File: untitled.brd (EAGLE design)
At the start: 41.6 x 28.6 mm, 21 parts, among them IC1 ACS758LCB-050B-PFF-T

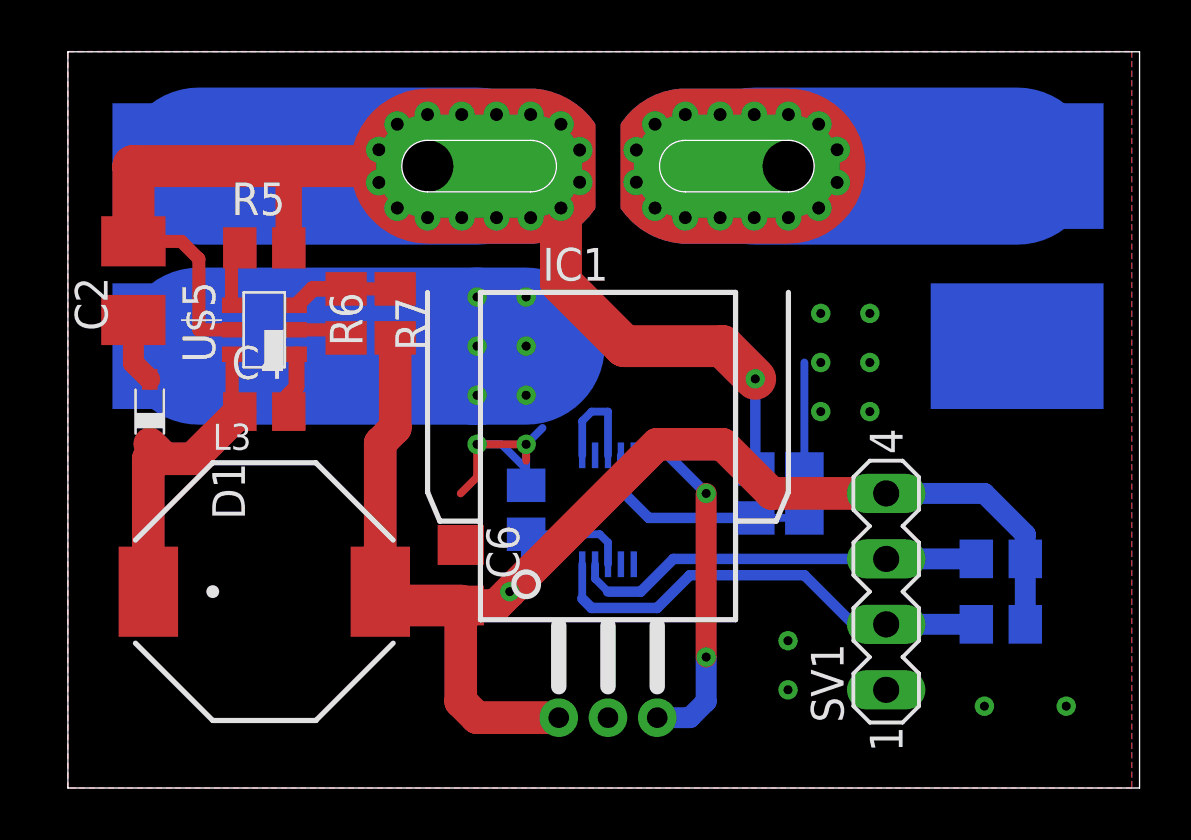
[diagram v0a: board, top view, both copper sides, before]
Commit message: Add TVS to power module
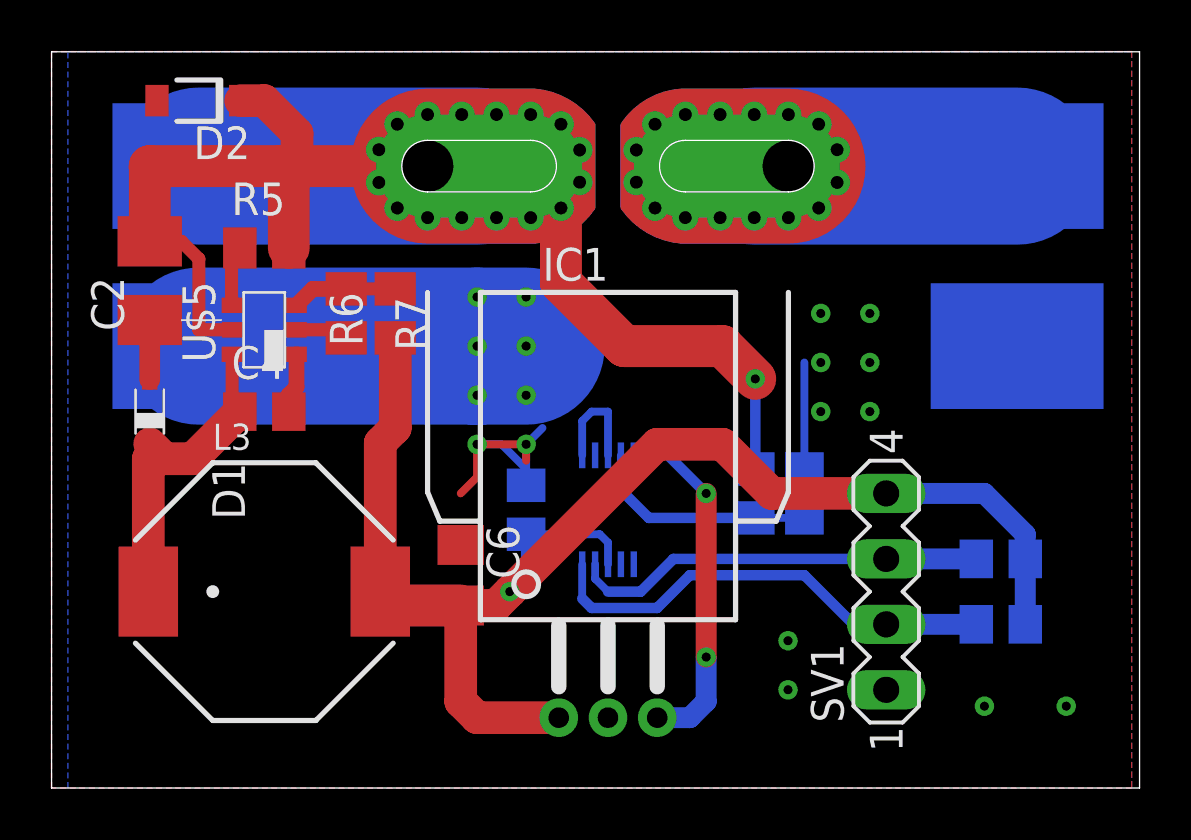
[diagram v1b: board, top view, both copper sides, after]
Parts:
- added D2: SMF5.0AT1, diode:SOD123FL
- moved C2 0.63 mm to (19.7, 34.9)
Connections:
- net GND: now also D2.A
- net N$4: now also D2.C
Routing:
- net N$4: track 58.3 -> 71.0 mm
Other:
- board size 41.6 x 28.6 mm -> 42.2 x 28.6 mm
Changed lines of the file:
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@@
 <layer number="18" name="Vias" color="2" fill="1" visible="yes" active="yes"/>
 <layer number="19" name="Unrouted" color="6" fill="1" visible="yes" active="yes"/>
-<layer number="20" name="Dimension" color="24" fill="1" visible="no" active="yes"/>
+<layer number="20" name="Dimension" color="24" fill="1" visible="yes" active="yes"/>
 <layer number="21" name="tPlace" color="7" fill="1" visible="yes" active="yes"/>
 <layer number="22" name="bPlace" color="7" fill="1" visible="yes" active="yes"/>
 <layer number="23" name="tOrigins" color="15" fill="1" visible="yes" active="yes"/>
 <layer number="24" name="bOrigins" color="15" fill="1" visible="yes" active="yes"/>
-<layer number="25" name="tNames" color="7" fill="1" visible="no" active="yes"/>
-<layer number="26" name="bNames" color="7" fill="1" visible="no" active="yes"/>
-<layer number="27" name="tValues" color="7" fill="1" visible="no" active="yes"/>
+<layer number="25" name="tNames" color="7" fill="1" visible="yes" active="yes"/>
+<layer number="26" name="bNames" color="7" fill="1" visible="yes" active="yes"/>
+<layer number="27" name="tValues" color="7" fill="1" visible="yes" active="yes"/>
 <layer number="28" name="bValues" color="7" fill="1" visible="no" active="yes"/>
 <layer number="29" name="tStop" color="7" fill="3" visible="no" active="yes"/>
@@
 <board>
 <plain>
-<wire x1="16.51" y1="15.24" x2="58.09" y2="15.24" width="0" layer="20"/>
+<wire x1="15.875" y1="15.24" x2="58.09" y2="15.24" width="0" layer="20"/>
 <wire x1="58.09" y1="15.24" x2="58.09" y2="43.805" width="0" layer="20"/>
-<wire x1="58.09" y1="43.805" x2="16.51" y2="43.805" width="0" layer="20"/>
-<wire x1="16.51" y1="43.805" x2="16.51" y2="15.24" width="0" layer="20"/>
+<wire x1="58.09" y1="43.805" x2="15.875" y2="43.805" width="0" layer="20"/>
+<wire x1="15.875" y1="43.805" x2="15.875" y2="15.24" width="0" layer="20"/>
 <text x="15.24" y="19.05" size="1.778" layer="26" ratio="18" rot="MR0" align="bottom-right">esk8pal
 v0.1.0
@@
 <attribute name="VALUE" x="21.685" y="28.195" size="1.27" layer="27" rot="R90"/>
 </element>
-<element name="C2" library="rcl" library_urn="urn:adsk.eagle:library:334" package="B/3528-21R" package3d_urn="urn:adsk.eagle:package:23409/2" value="2.2uF 100V" x="19.05" y="34.925" smashed="yes" rot="R90">
-<attribute name="NAME" x="18.05" y="32.975" size="1.27" layer="25" rot="R90"/>
-<attribute name="POPULARITY" value="1" x="19.05" y="34.925" size="1.778" layer="27" rot="R90" display="off"/>
-<attribute name="SPICEPREFIX" value="C" x="19.05" y="34.925" size="1.778" layer="27" rot="R90" display="off"/>
-<attribute name="VALUE" x="21.375" y="32.975" size="1.27" layer="27" rot="R90"/>
+<element name="C2" library="rcl" library_urn="urn:adsk.eagle:library:334" package="B/3528-21R" package3d_urn="urn:adsk.eagle:package:23409/2" value="2.2uF 100V" x="19.685" y="34.925" smashed="yes" rot="R90">
+<attribute name="NAME" x="18.685" y="32.975" size="1.27" layer="25" rot="R90"/>
+<attribute name="POPULARITY" value="1" x="19.685" y="34.925" size="1.778" layer="27" rot="R90" display="off"/>
+<attribute name="SPICEPREFIX" value="C" x="19.685" y="34.925" size="1.778" layer="27" rot="R90" display="off"/>
+<attribute name="VALUE" x="22.01" y="32.975" size="1.27" layer="27" rot="R90"/>
 </element>
 <element name="C6" library="rcl" library_urn="urn:adsk.eagle:library:334" package="R/2012-12R" package3d_urn="urn:adsk.eagle:package:23426/2" value="22uF 25V" x="31.75" y="23.495" smashed="yes" rot="R270">
@@
 <attribute name="NAME" x="22.13" y="28.36" size="1.016" layer="25" ratio="18"/>
 <attribute name="VALUE" x="22.13" y="16.61" size="0.8128" layer="27" ratio="10"/>
+</element>
+<element name="D2" library="diode" library_urn="urn:adsk.eagle:library:210" package="SOD123FL" package3d_urn="urn:adsk.eagle:package:43458/1" value="SMF5.0AT1" x="21.59" y="41.91" smashed="yes" rot="R180">
+<attribute name="NAME" x="23.59" y="40.91" size="1.27" layer="25" rot="R180"/>
+<attribute name="POPULARITY" value="2" x="21.59" y="41.91" size="1.778" layer="27" rot="R180" display="off"/>
+<attribute name="VALUE" x="23.59" y="44.41" size="1.27" layer="27" rot="R180"/>
 </element>
 </elements>
@@
 <contactref element="C2" pad="-"/>
 <contactref element="C6" pad="-"/>
-<wire x1="19.05" y1="33.4" x2="19.05" y2="31.73" width="0.8128" layer="1"/>
-<wire x1="19.05" y1="31.73" x2="19.685" y2="31.095" width="0.8128" layer="1"/>
+<wire x1="19.685" y1="33.4" x2="19.685" y2="31.095" width="0.8128" layer="1"/>
 <wire x1="25.38" y1="33.02" x2="26.99" y2="33.02" width="0.508" layer="1"/>
 <wire x1="26.99" y1="33.02" x2="27.305" y2="32.705" width="0.508" layer="1"/>
 <polygon width="0.508" layer="1" isolate="0.4064">
-<vertex x="16.51" y="43.815"/>
+<vertex x="15.875" y="43.815"/>
 <vertex x="57.785" y="43.815"/>
 <vertex x="57.785" y="15.24"/>
-<vertex x="16.51" y="15.24"/>
+<vertex x="15.875" y="15.24"/>
 </polygon>
 <wire x1="34.29" y1="32.385" x2="32.385" y2="32.385" width="6.096" layer="16"/>
@@
 <via x="47.625" y="29.845" extent="1-16" drill="0.35"/>
 <via x="45.72" y="29.845" extent="1-16" drill="0.35"/>
+<contactref element="D2" pad="A"/>
 </signal>
 <signal name="VCC">
@@
 <contactref element="R5" pad="2"/>
 <contactref element="U$5" pad="5"/>
-<wire x1="33.02" y1="38.735" x2="31.115" y2="40.64" width="1.016" layer="1"/>
+<wire x1="33.02" y1="38.735" x2="32.0675" y2="39.6875" width="1.016" layer="1"/>
 <contactref element="C2" pad="+"/>
+<wire x1="32.0675" y1="39.6875" x2="31.115" y2="40.64" width="1.016" layer="1"/>
 <wire x1="21.59" y1="39.37" x2="32.385" y2="39.37" width="6.096" layer="16"/>
 <wire x1="35.64" y1="37.745" x2="35.64" y2="34.845" width="1.6256" layer="1"/>
 <wire x1="35.64" y1="34.845" x2="38.1" y2="32.385" width="1.6256" layer="1"/>
-<wire x1="30.465" y1="39.37" x2="25.08" y2="39.37" width="1.6256" layer="1"/>
-<wire x1="24.765" y1="39.37" x2="19.05" y2="39.37" width="1.6256" layer="1"/>
-<wire x1="19.05" y1="39.37" x2="19.05" y2="36.45" width="1.6256" layer="1"/>
+<wire x1="19.685" y1="36.45" x2="19.685" y2="39.37" width="1.6256" layer="1"/>
 <wire x1="22.88" y1="33.02" x2="21.59" y2="33.02" width="0.508" layer="1"/>
-<wire x1="20.91" y1="36.45" x2="19.05" y2="36.45" width="0.508" layer="1"/>
+<wire x1="20.91" y1="36.45" x2="19.685" y2="36.45" width="0.508" layer="1"/>
 <wire x1="21.59" y1="35.77" x2="20.91" y2="36.45" width="0.508" layer="1"/>
 <wire x1="21.59" y1="33.02" x2="21.59" y2="35.77" width="0.508" layer="1"/>
@@
 <wire x1="41.91" y1="32.385" x2="38.1" y2="32.385" width="1.6256" layer="1"/>
 <wire x1="43.18" y1="27.62" x2="43.18" y2="31.115" width="0.4064" layer="16"/>
-<wire x1="25.08" y1="36.195" x2="25.08" y2="39.37" width="1.016" layer="1"/>
+<wire x1="25.08" y1="36.195" x2="25.08" y2="39.37" width="1.6256" layer="1"/>
+<contactref element="D2" pad="C"/>
+<wire x1="19.685" y1="39.37" x2="22.225" y2="39.37" width="1.6256" layer="1"/>
+<wire x1="33.02" y1="39.37" x2="33.655" y2="39.37" width="1.6256" layer="1"/>
+<wire x1="24.765" y1="39.37" x2="25.4" y2="39.37" width="1.6256" layer="1"/>
+<wire x1="25.4" y1="39.37" x2="31.115" y2="39.37" width="0.508" layer="1"/>
+<wire x1="31.115" y1="39.37" x2="33.02" y2="39.37" width="0.508" layer="1"/>
+<wire x1="22.225" y1="39.37" x2="24.765" y2="39.37" width="1.6256" layer="1"/>
+<wire x1="31.75" y1="39.37" x2="32.0675" y2="39.6875" width="1.27" layer="1"/>
+<wire x1="23.215" y1="41.91" x2="24.13" y2="41.91" width="1.27" layer="1"/>
+<wire x1="25.4" y1="40.64" x2="25.4" y2="39.37" width="1.27" layer="1"/>
+<wire x1="24.13" y1="41.91" x2="25.4" y2="40.64" width="1.27" layer="1"/>
+<wire x1="25.08" y1="39.37" x2="31.115" y2="39.37" width="1.6256" layer="1"/>
 <wire x1="33.655" y1="38.735" x2="33.02" y2="38.735" width="0" layer="19" extent="1-16"/>
-<wire x1="24.765" y1="39.37" x2="21.59" y2="39.37" width="0" layer="19" extent="1-16"/>
+<wire x1="33.655" y1="39.37" x2="33.655" y2="38.735" width="0" layer="19" extent="1-16"/>
 </signal>
 <signal name="N$5">

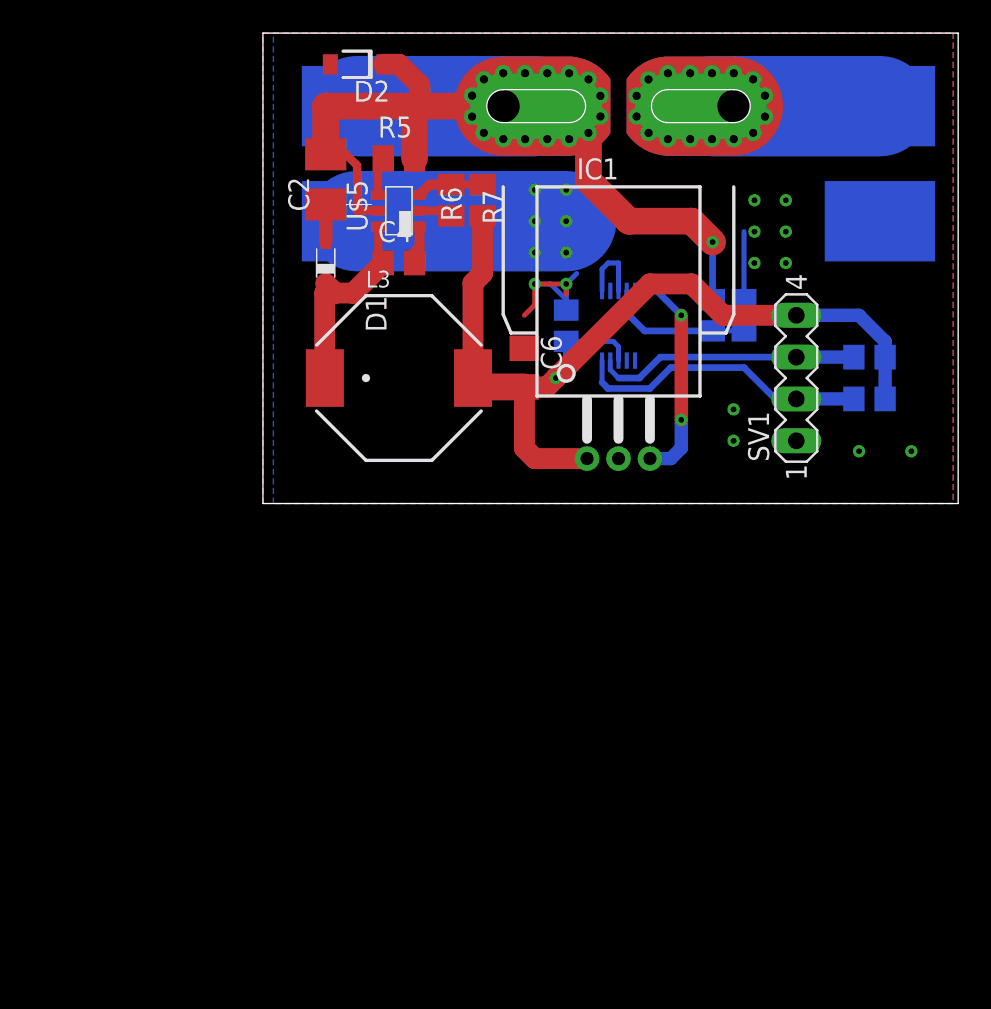
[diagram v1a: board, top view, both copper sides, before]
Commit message: Update scheamictic to include dedicated ldo for senors and p mosfeto control power for sensors
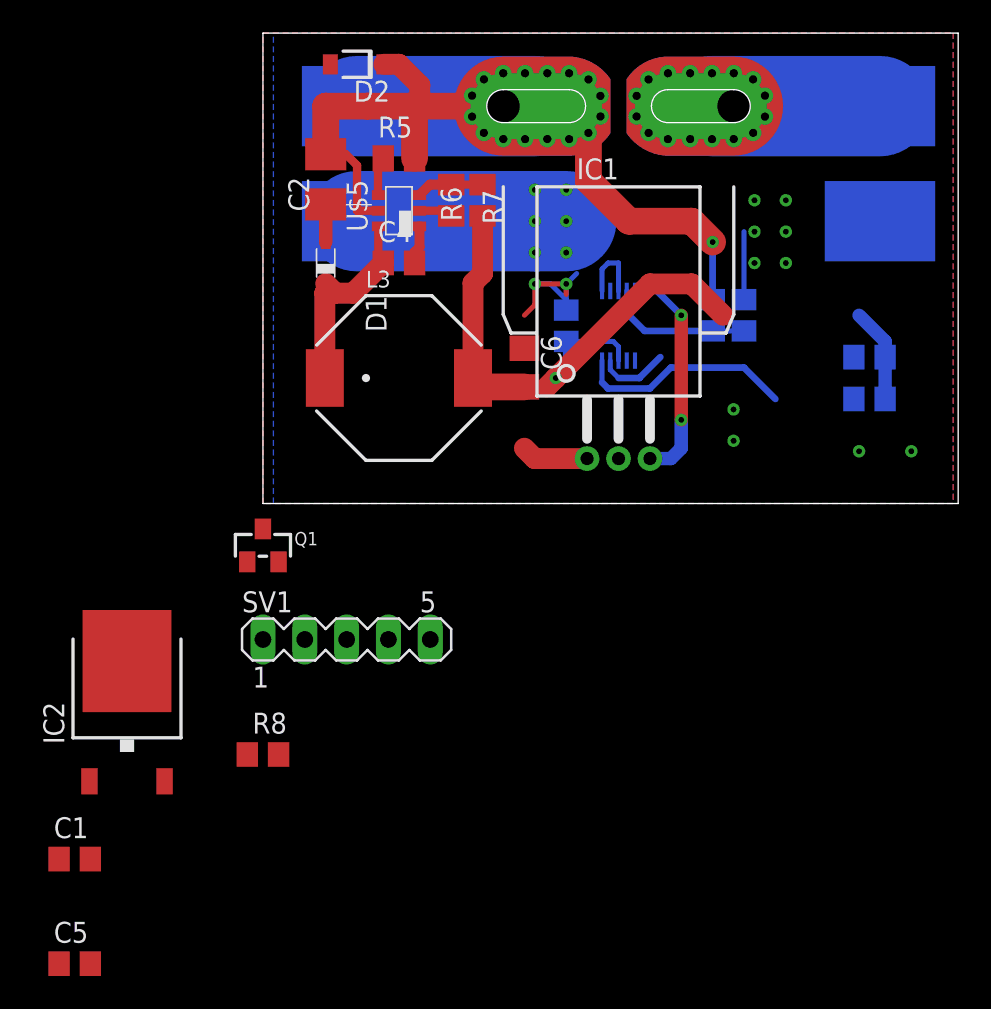
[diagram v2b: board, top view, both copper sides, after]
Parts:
- added C1, C5: 100nF, rcl:C0805
- added IC2: LM2936DT-3.3, national-semiconductor:TO252
- added Q1: (no value), microbuilder:SOT23-WIDE
- added R8: 100k, rcl:R0805
- SV1: device con-lstb:MA04-1 -> con-lstb:MA05-1
- moved SV1 31.6 mm to (21.0, 6.99), turned to 0 degrees
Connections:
- new net N$12: C1.1, IC2.3, Q1.2, R8.1
- new net N$7: Q1.1, R8.2, SV1.5
- new net N$8: C6.+, L3.2, R6.1, SV1.4
- net GND: now also C1.2, C5.2, IC2.2
- net N$4: now also C5.1, IC2.1
- net VCC: now also Q1.3; no longer C6.+, L3.2, R6.1, SV1.4
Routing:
- net VCC: track 57.5 -> 30.5 mm
- net N$8: track 0.00 -> 13.7 mm
- net N$5: track 16.1 -> 4.34 mm
- net N$6: track 18.1 -> 13.3 mm

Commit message: Update board layout for new components
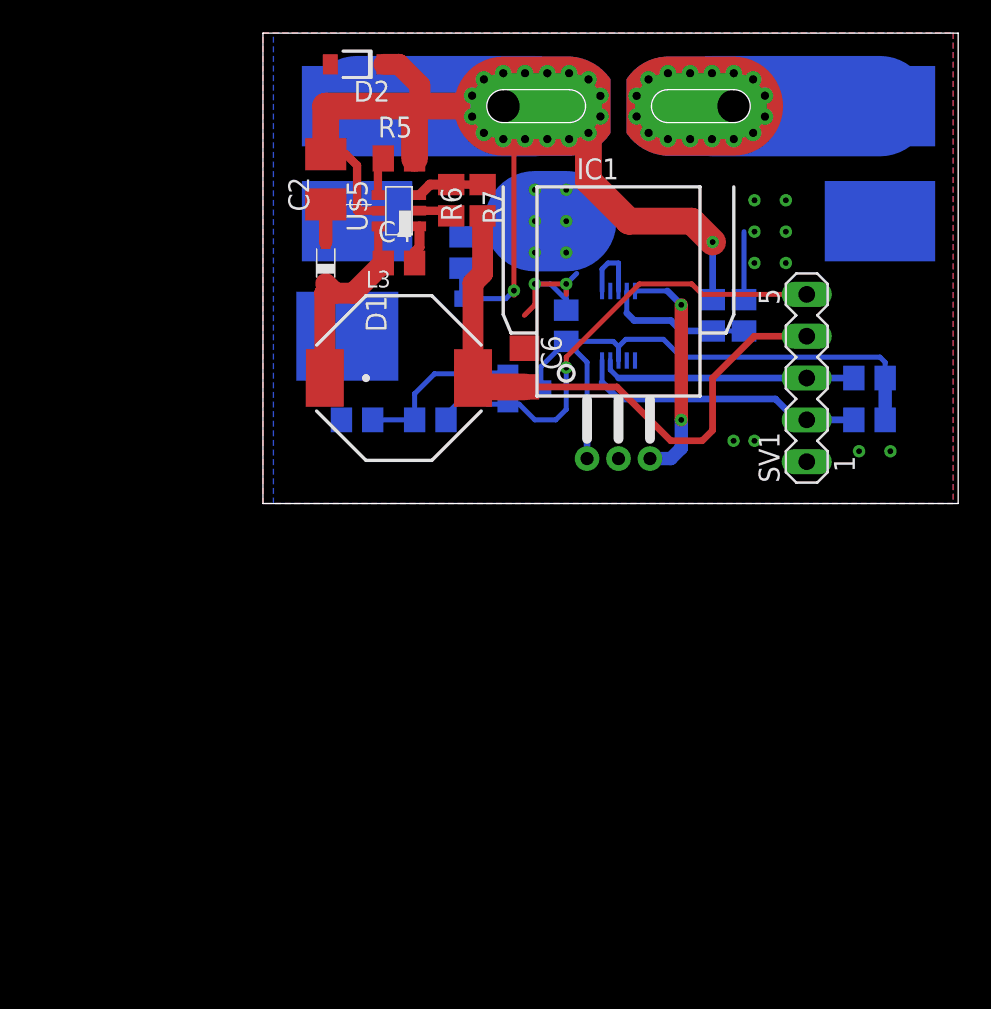
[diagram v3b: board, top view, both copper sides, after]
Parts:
- moved C5 49.2 mm to (27.9, 30.5), flipped to the bottom, turned to 90 degrees
- moved SV1 32.1 mm to (48.9, 22.9), turned to 90 degrees
- moved C1 31.7 mm to (21.6, 20.3), flipped to the bottom
- moved IC2 27.3 mm to (23.5, 25.4), flipped to the bottom, turned to 270 degrees
- moved R8 22.7 mm to (26.0, 20.3), flipped to the bottom, turned to 180 degrees
- moved Q1 18.5 mm to (31.8, 22.2), flipped to the bottom, turned to 90 degrees
- moved R3 1.27 mm to (52.7, 20.3)
- moved R4 1.27 mm to (52.7, 22.9)
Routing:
- net N$7: track 0.00 -> 28.7 mm, vias 0 -> 1
- net N$8: track 13.7 -> 36.7 mm
- net N$4: track 71.0 -> 89.2 mm, vias 1 -> 2
- net N$5: track 4.34 -> 15.6 mm
- net GND: track 35.5 -> 24.7 mm
- net N$12: track 0.00 -> 10.3 mm
- net VCC: track 30.5 -> 37.2 mm, vias 1 -> 0
- net N$6: track 13.3 -> 17.6 mm
